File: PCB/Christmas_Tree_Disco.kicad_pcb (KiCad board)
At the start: 2 copper layers, 190.5 x 188.9 mm, 137 parts, among them J1 PJ-006B-SMT-TR, U1 DEV_KIT_EK-TM4C123GXL, U2 TLC5955DCA, U3 LM1085-5.0, U4 MC14504B

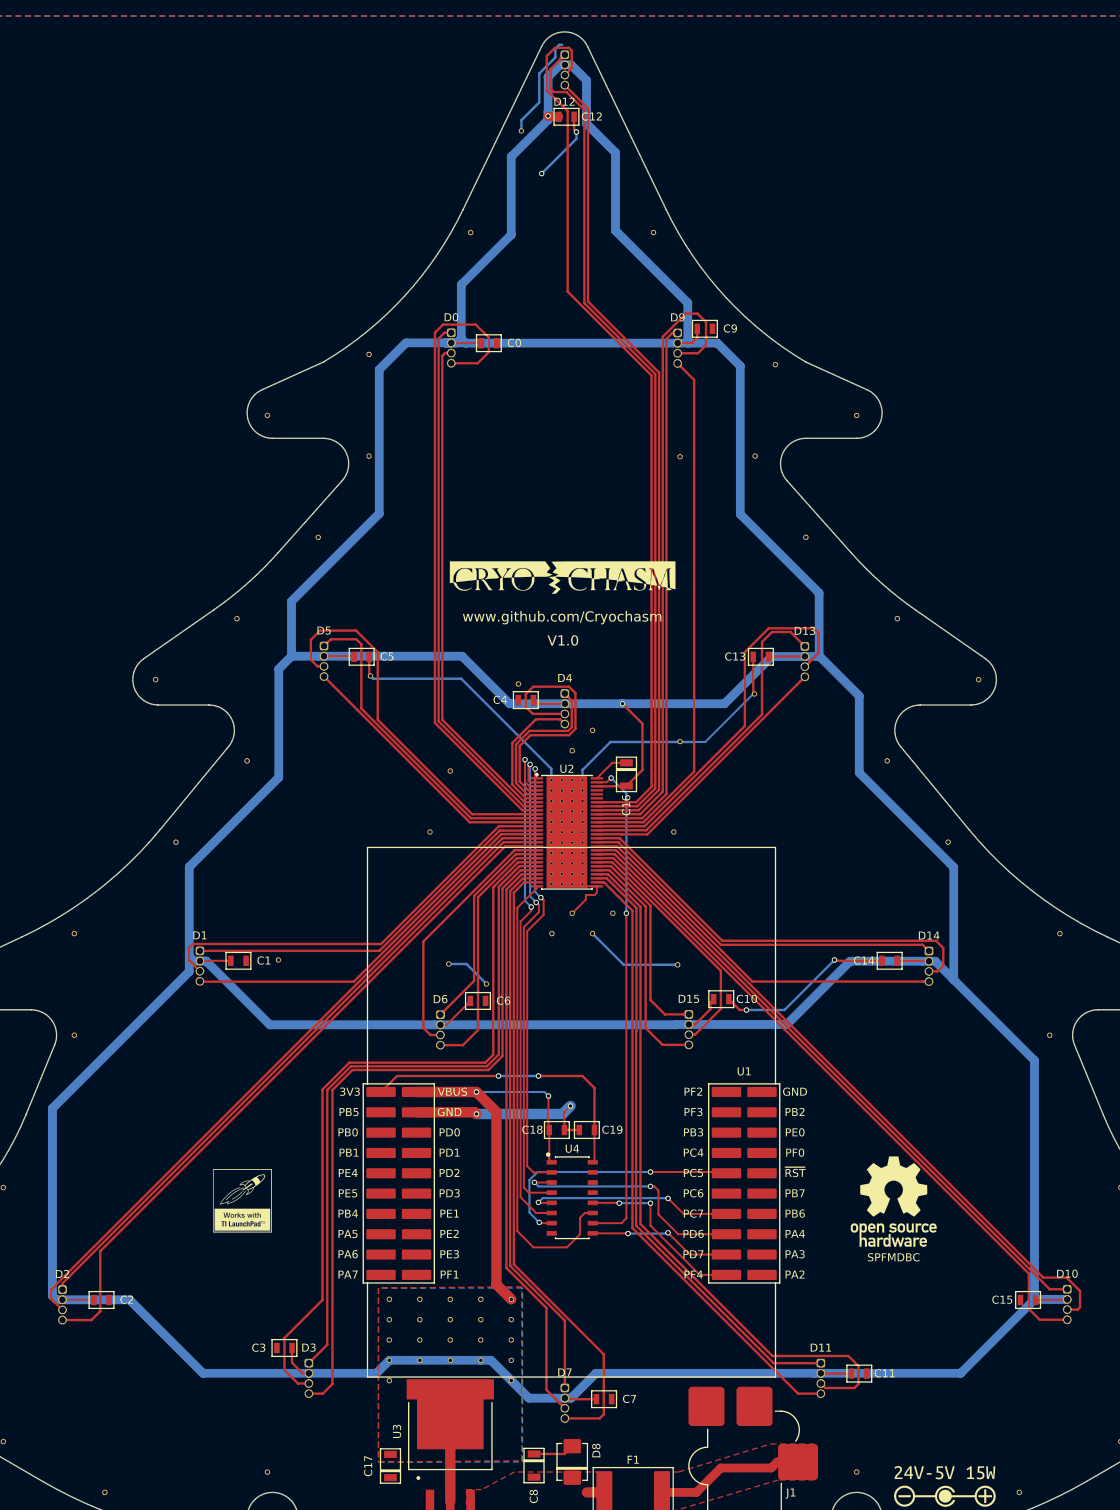
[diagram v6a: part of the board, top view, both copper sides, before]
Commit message: Removed Level Shifter, Cleaned up gerbers
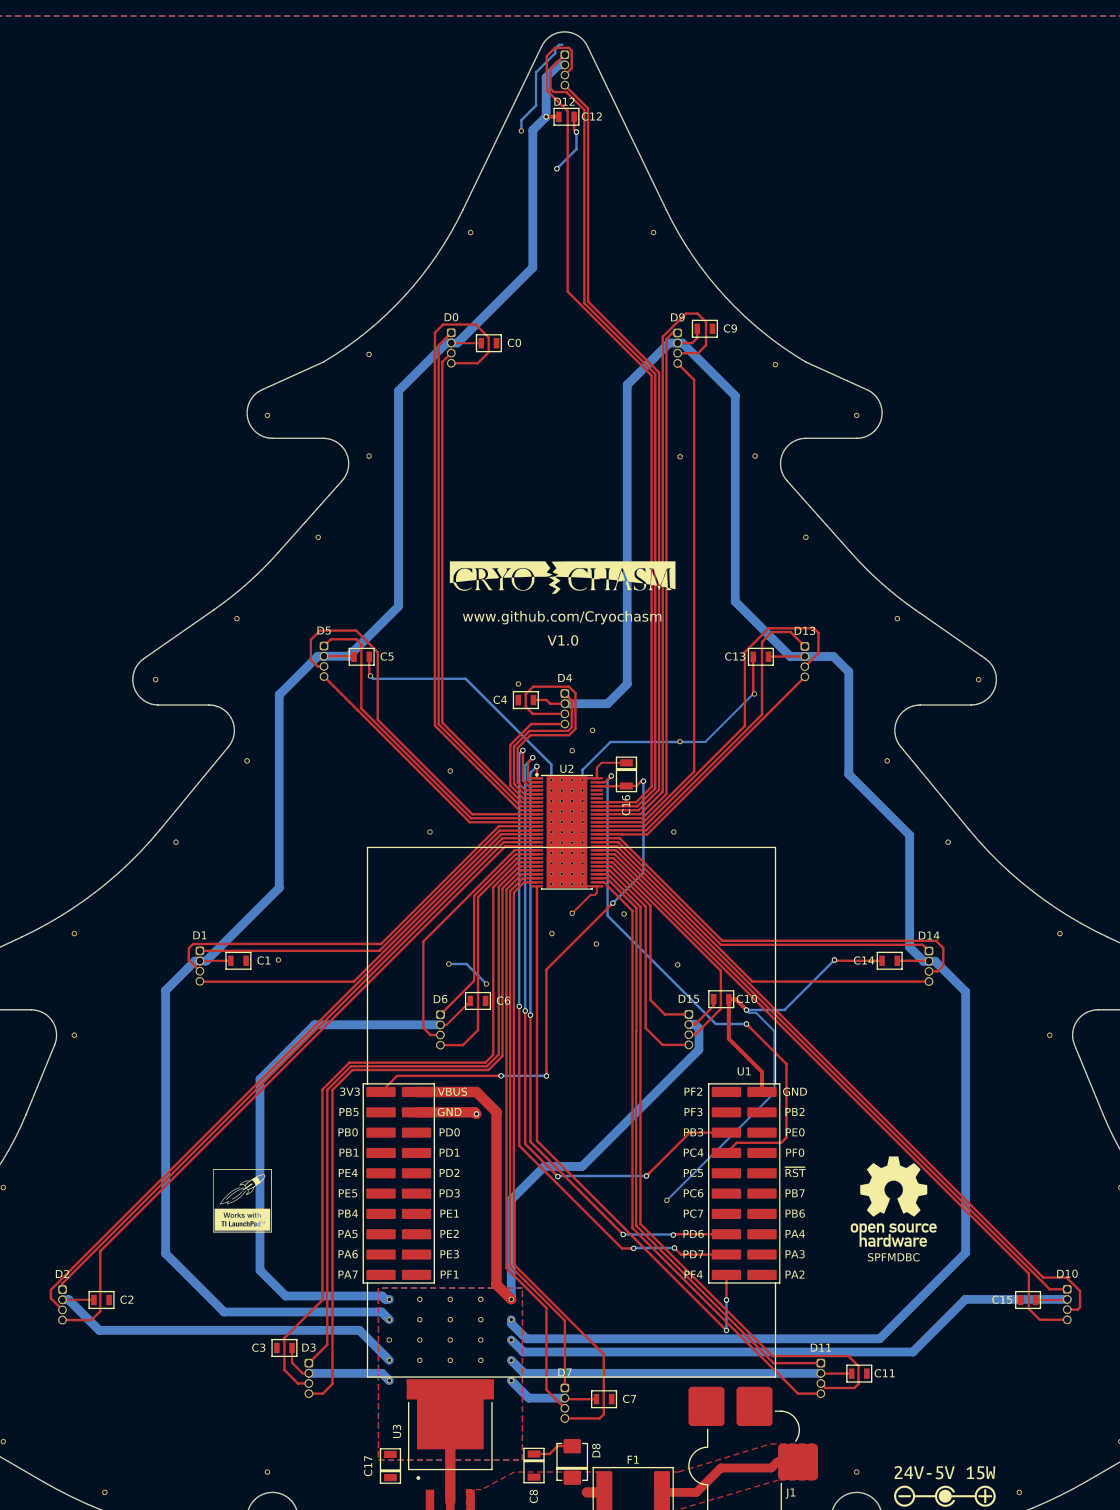
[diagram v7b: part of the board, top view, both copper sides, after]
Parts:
- removed C18, C19: 0.1u, local:SMD-0805
- removed U4: MC14504B, local:SOIC-16
- added STITCH: VIA-432-686, local:VIA-432-686, F.Cu at (121.0, 173.1)
- moved STITCH 1.40 mm to (115.7, 137.2)
- moved STITCH 1.39 mm to (112.2, 141.0)
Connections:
- C16 pad 2: /Top Sheet/Microcontroller/5V -> /Top Sheet/Microcontroller/3V3
- U1 pad 23: Net-(U1-Pad23) -> /Top Sheet/Microcontroller/SCLK
- U1 pad 24: Net-(U1-Pad24) -> /Top Sheet/Microcontroller/GSCLK
- U1 pad 25: /Top Sheet/Microcontroller/LAT_3V3 -> (no net)
- U1 pad 27: /Top Sheet/Microcontroller/SCLK_3V3 -> (no net)
- U1 pad 28: /Top Sheet/Microcontroller/DATA_3V3 -> /Top Sheet/Microcontroller/DATA
- U1 pad 29: /Top Sheet/Microcontroller/GSCLK_3V3 -> /Top Sheet/Microcontroller/LAT
- U1 pad 30: /Top Sheet/Microcontroller/ERROR_RD_3V3 -> /Top Sheet/Microcontroller/ERROR_RD
- U2 pad 54: /Top Sheet/Microcontroller/5V -> /Top Sheet/Microcontroller/3V3
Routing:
- net /Top Sheet/Microcontroller/LAT_3V3: track 32.5 -> 0.00 mm, vias 2 -> 0
- net /Top Sheet/Microcontroller/3V3: track 37.5 -> 69.5 mm, vias 2 -> 4
- net /Top Sheet/Microcontroller/DATA_3V3: track 30.6 -> 0.00 mm, vias 2 -> 0
- net /Top Sheet/Microcontroller/SCLK_3V3: track 26.2 -> 0.00 mm, vias 2 -> 0
- net /Top Sheet/Microcontroller/DATA: track 55.6 -> 78.1 mm, vias 2 -> 4
- net /Top Sheet/Microcontroller/LAT: track 64.8 -> 87.0 mm, vias 2 -> 4
- net /Top Sheet/Microcontroller/ERROR_RD_3V3: track 22.1 -> 0.00 mm, vias 2 -> 0
- net /Top Sheet/Microcontroller/SCLK: track 61.2 -> 82.1 mm, vias 2 -> 4
- net /Top Sheet/Microcontroller/GSCLK_3V3: track 17.9 -> 0.00 mm, vias 2 -> 0
- net /Top Sheet/Microcontroller/GND: track 168.2 -> 184.6 mm, vias 6 -> 5
- net /Top Sheet/Microcontroller/ERROR_RD: track 57.4 -> 72.3 mm, vias 0 -> 2
- net /Top Sheet/Microcontroller/GSCLK: track 62.3 -> 67.3 mm
- net /Top Sheet/Microcontroller/5V: track 847.7 -> 848.8 mm, vias 4 -> 1

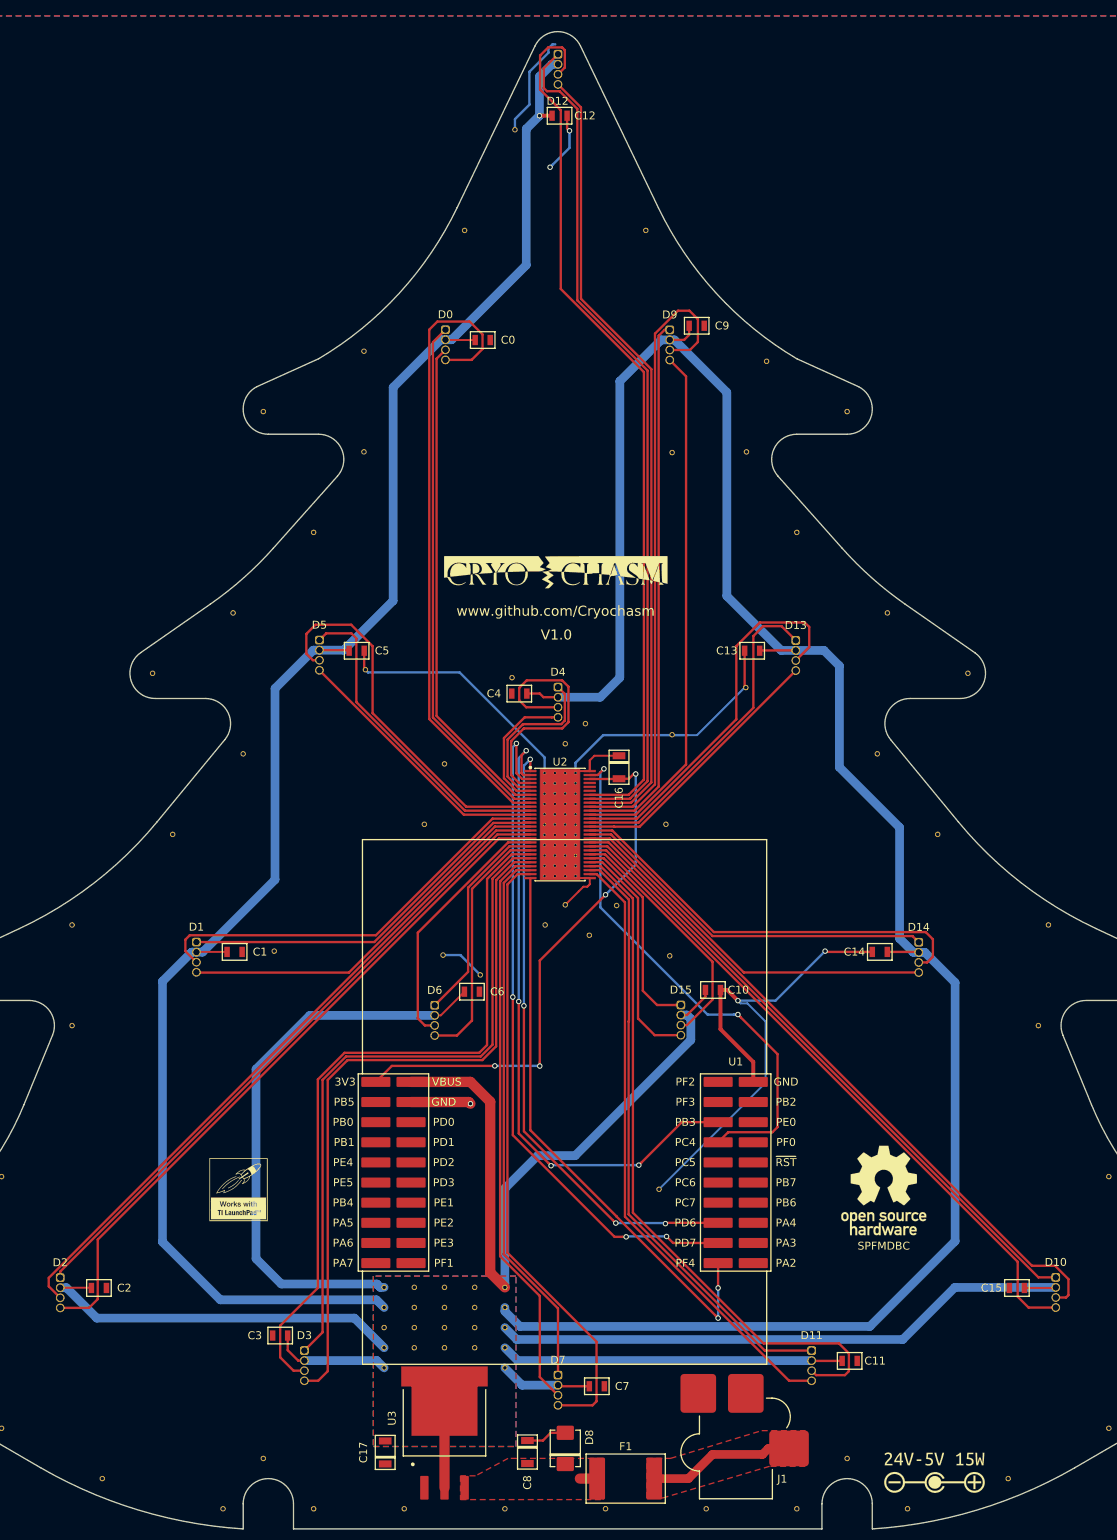
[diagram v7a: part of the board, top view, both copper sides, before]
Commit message: Footprint Modifications
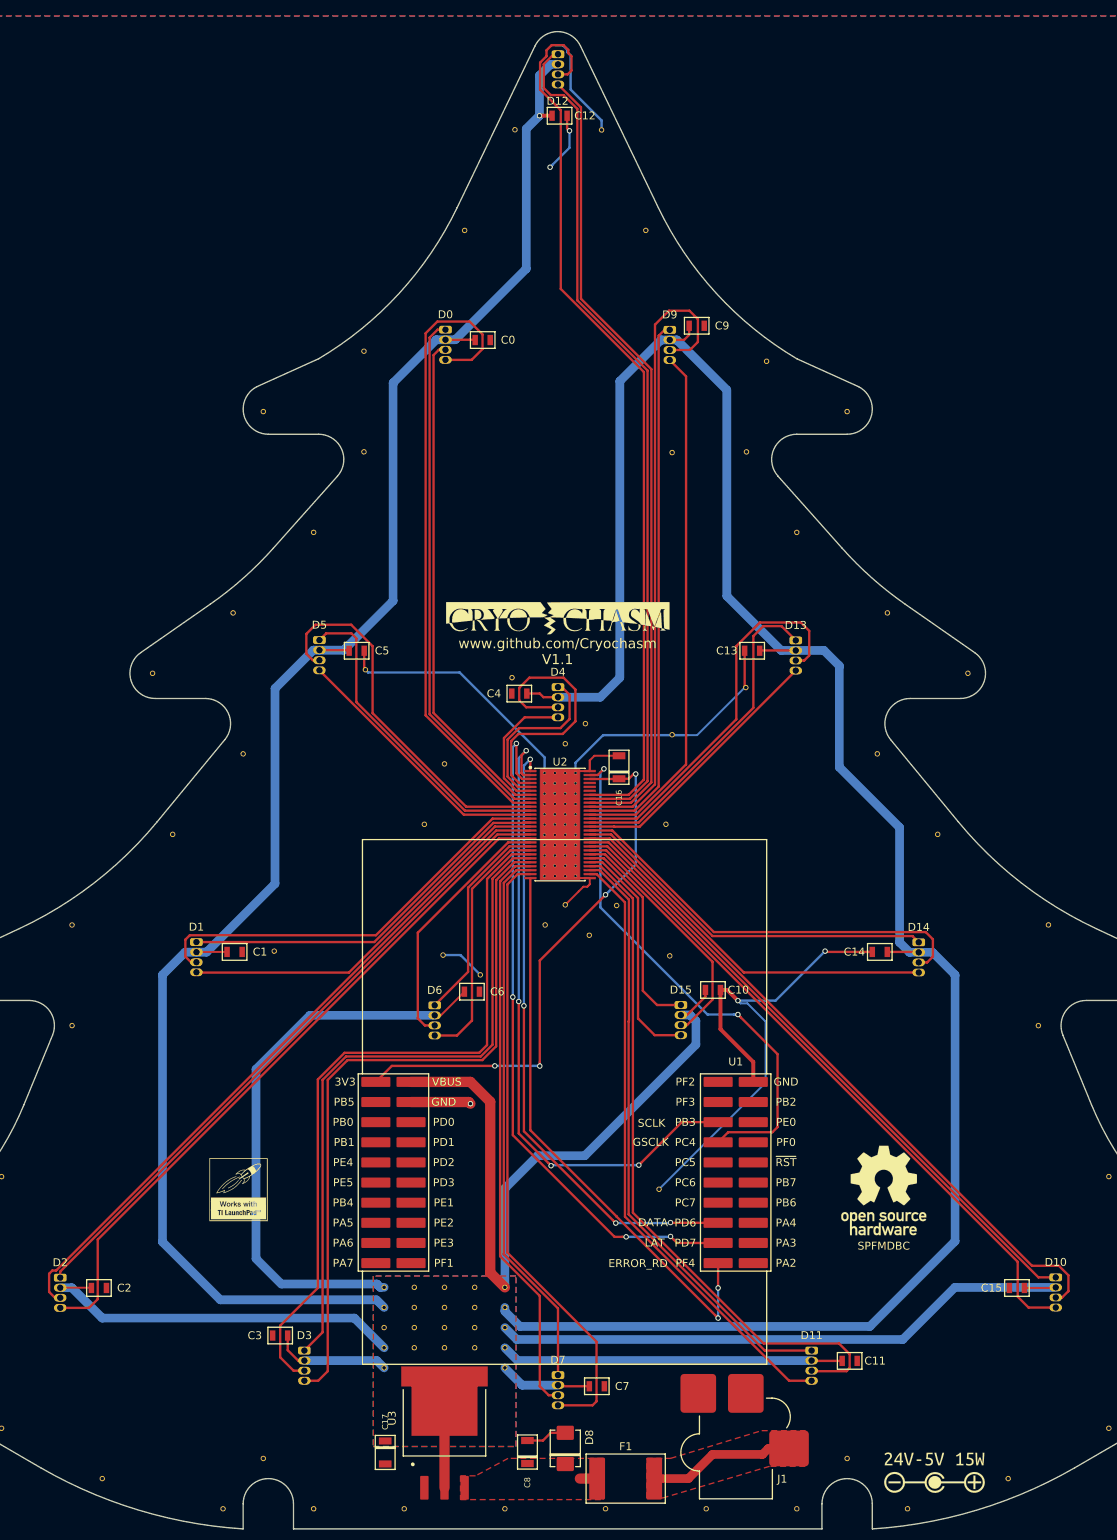
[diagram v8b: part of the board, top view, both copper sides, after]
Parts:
- removed V1.0: www.github.com/Cryochasm, local:Cryochasm
- added STITCH: VIA-432-686, local:VIA-432-686, F.Cu at (113.8, 39.4)
- added V1.1: www.github.com/Cryochasm, local:Cryochasm, F.Cu at (108.2, 101.0)
- C16, C17, C8: footprint local:SMD-POL-1206 -> local:SMD-TANT-1206
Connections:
- J1 pad 3: Net-(J1-Pad3) -> (no net)
- U1 pad 10: Net-(U1-Pad10) -> (no net)
- U1 pad 11: Net-(U1-Pad11) -> (no net)
- U1 pad 12: Net-(U1-Pad12) -> (no net)
- U1 pad 13: Net-(U1-Pad13) -> (no net)
- U1 pad 14: Net-(U1-Pad14) -> (no net)
- U1 pad 15: Net-(U1-Pad15) -> (no net)
- U1 pad 16: Net-(U1-Pad16) -> (no net)
- U1 pad 17: Net-(U1-Pad17) -> (no net)
- U1 pad 18: Net-(U1-Pad18) -> (no net)
- U1 pad 2: Net-(U1-Pad2) -> (no net)
- U1 pad 21: Net-(U1-Pad21) -> (no net)
- U1 pad 22: Net-(U1-Pad22) -> (no net)
- U1 pad 25: (no net) -> Net-(U1-Pad25)
- U1 pad 26: Net-(U1-Pad26) -> (no net)
- U1 pad 27: (no net) -> Net-(U1-Pad27)
- U1 pad 3: Net-(U1-Pad3) -> (no net)
- U1 pad 31: Net-(U1-Pad31) -> (no net)
- U1 pad 32: Net-(U1-Pad32) -> (no net)
- U1 pad 33: Net-(U1-Pad33) -> (no net)
- U1 pad 34: Net-(U1-Pad34) -> (no net)
- U1 pad 35: Net-(U1-Pad35) -> (no net)
- U1 pad 36: Net-(U1-Pad36) -> (no net)
- U1 pad 37: Net-(U1-Pad37) -> (no net)
- U1 pad 38: Net-(U1-Pad38) -> (no net)
- U1 pad 39: Net-(U1-Pad39) -> (no net)
- U1 pad 4: Net-(U1-Pad4) -> (no net)
- U1 pad 5: Net-(U1-Pad5) -> (no net)
- U1 pad 6: Net-(U1-Pad6) -> (no net)
- U1 pad 7: Net-(U1-Pad7) -> (no net)
- U1 pad 8: Net-(U1-Pad8) -> (no net)
- U1 pad 9: Net-(U1-Pad9) -> (no net)
- U2 pad 51: Net-(U2-Pad51) -> (no net)
- U2 pad 52: Net-(U2-Pad52) -> (no net)
- U2 pad 53: Net-(U2-Pad53) -> (no net)
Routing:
- net /Top Sheet/Microcontroller/5V: track 848.8 -> 852.8 mm
- net /Top Sheet/RGB LED Array/RGB12_0: track 111.5 -> 113.3 mm
- net /Top Sheet/RGB LED Array/RGB04_0: track 33.6 -> 35.3 mm
- net /Top Sheet/RGB LED Array/RGB00_1: track 66.1 -> 67.1 mm
- net /Top Sheet/RGB LED Array/RGB00_0: track 62.6 -> 63.4 mm
- net /Top Sheet/RGB LED Array/RGB07_0: track 72.5 -> 73.1 mm
- net /Top Sheet/RGB LED Array/RGB09_0: track 80.2 -> 80.8 mm
- net /Top Sheet/RGB LED Array/RGB02_0: track 87.2 -> 87.9 mm
- net /Top Sheet/Microcontroller/GND: track 184.6 -> 185.1 mm
- net /Top Sheet/RGB LED Array/RGB04_1: track 20.9 -> 21.4 mm
- net /Top Sheet/RGB LED Array/RGB11_0: track 88.8 -> 88.3 mm
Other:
- board text added: "DATA"
- board text added: "ERROR_RD"
- board text added: "GSCLK"
- board text added: "LAT"
- board text added: "SCLK"
